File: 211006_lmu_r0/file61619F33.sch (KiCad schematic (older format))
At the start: 28 parts

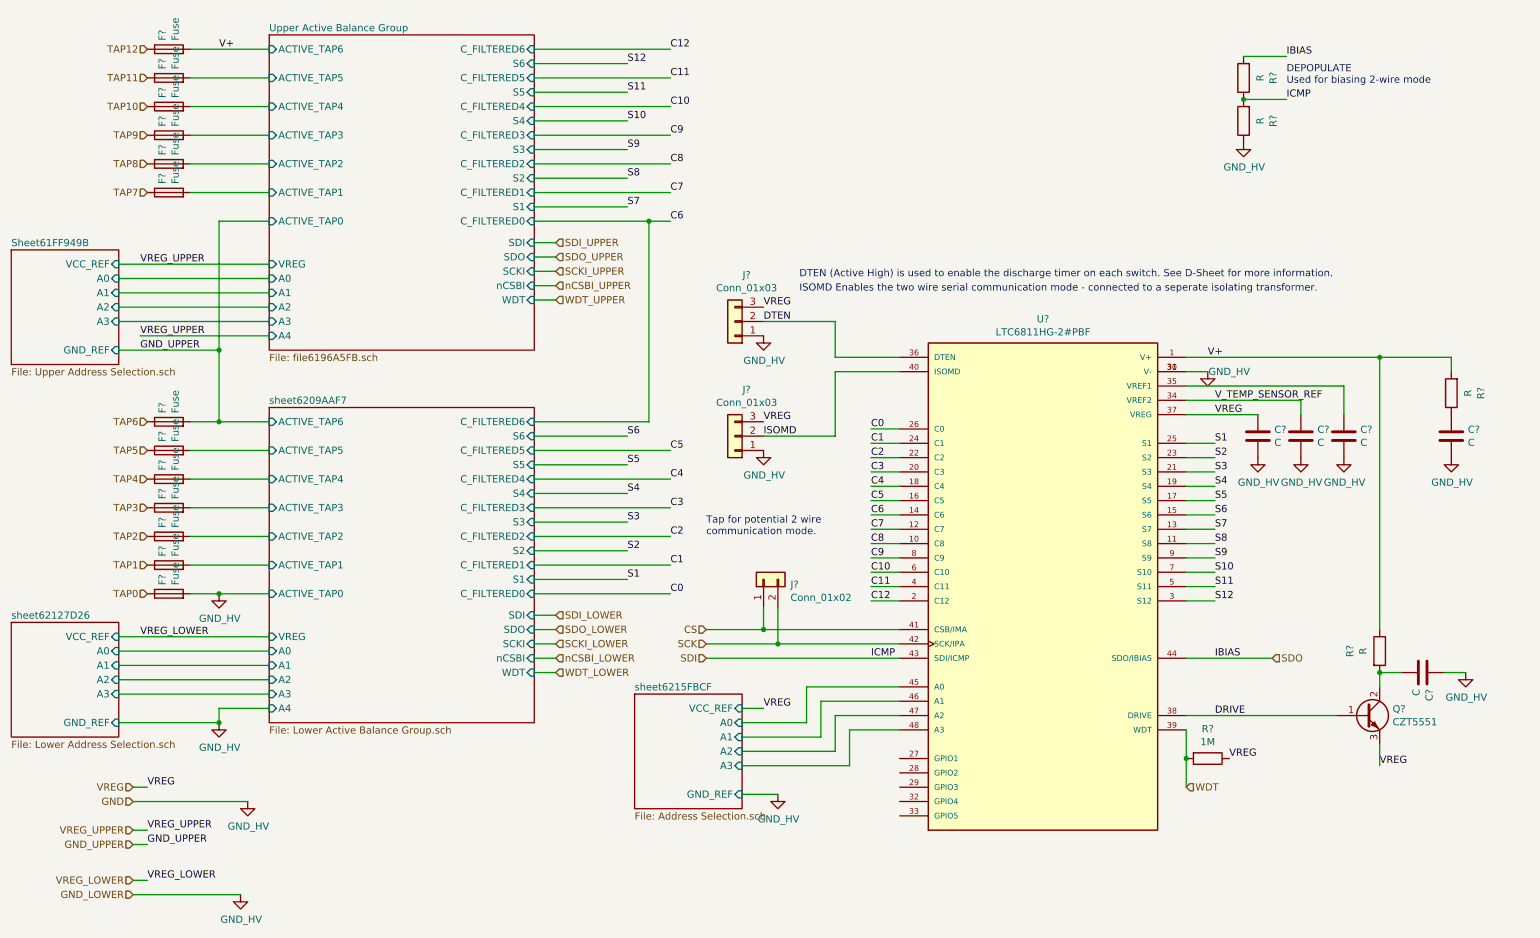
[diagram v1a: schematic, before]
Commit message: Updated BOM and footprints for non-hv components
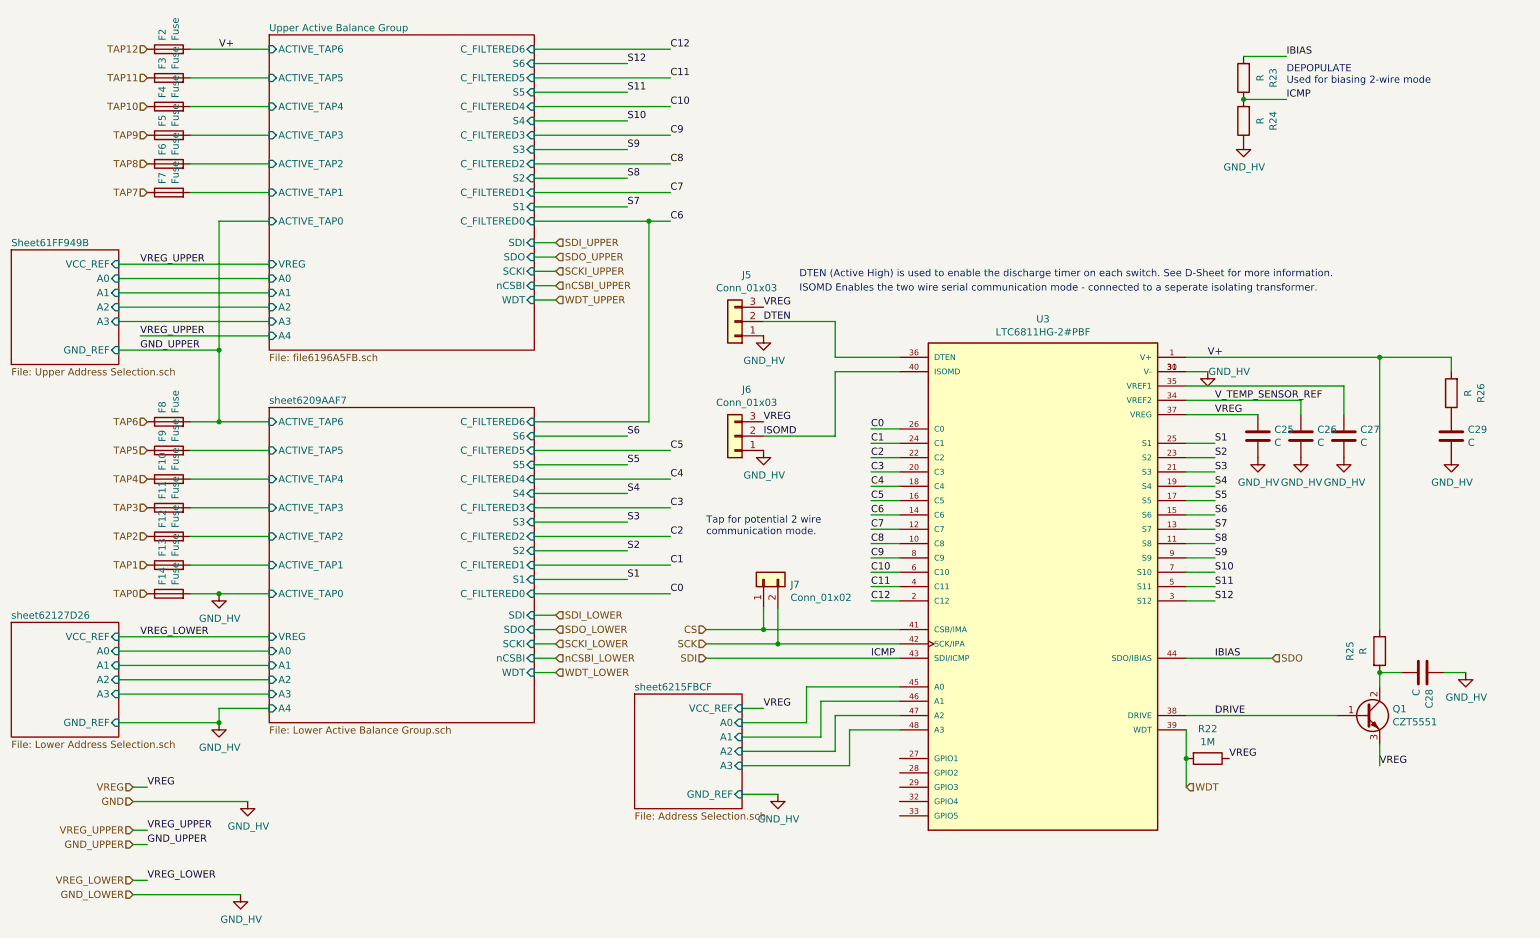
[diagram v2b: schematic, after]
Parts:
- gave numbers to parts that had none: 28

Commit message: Added most footprint requirements in HV
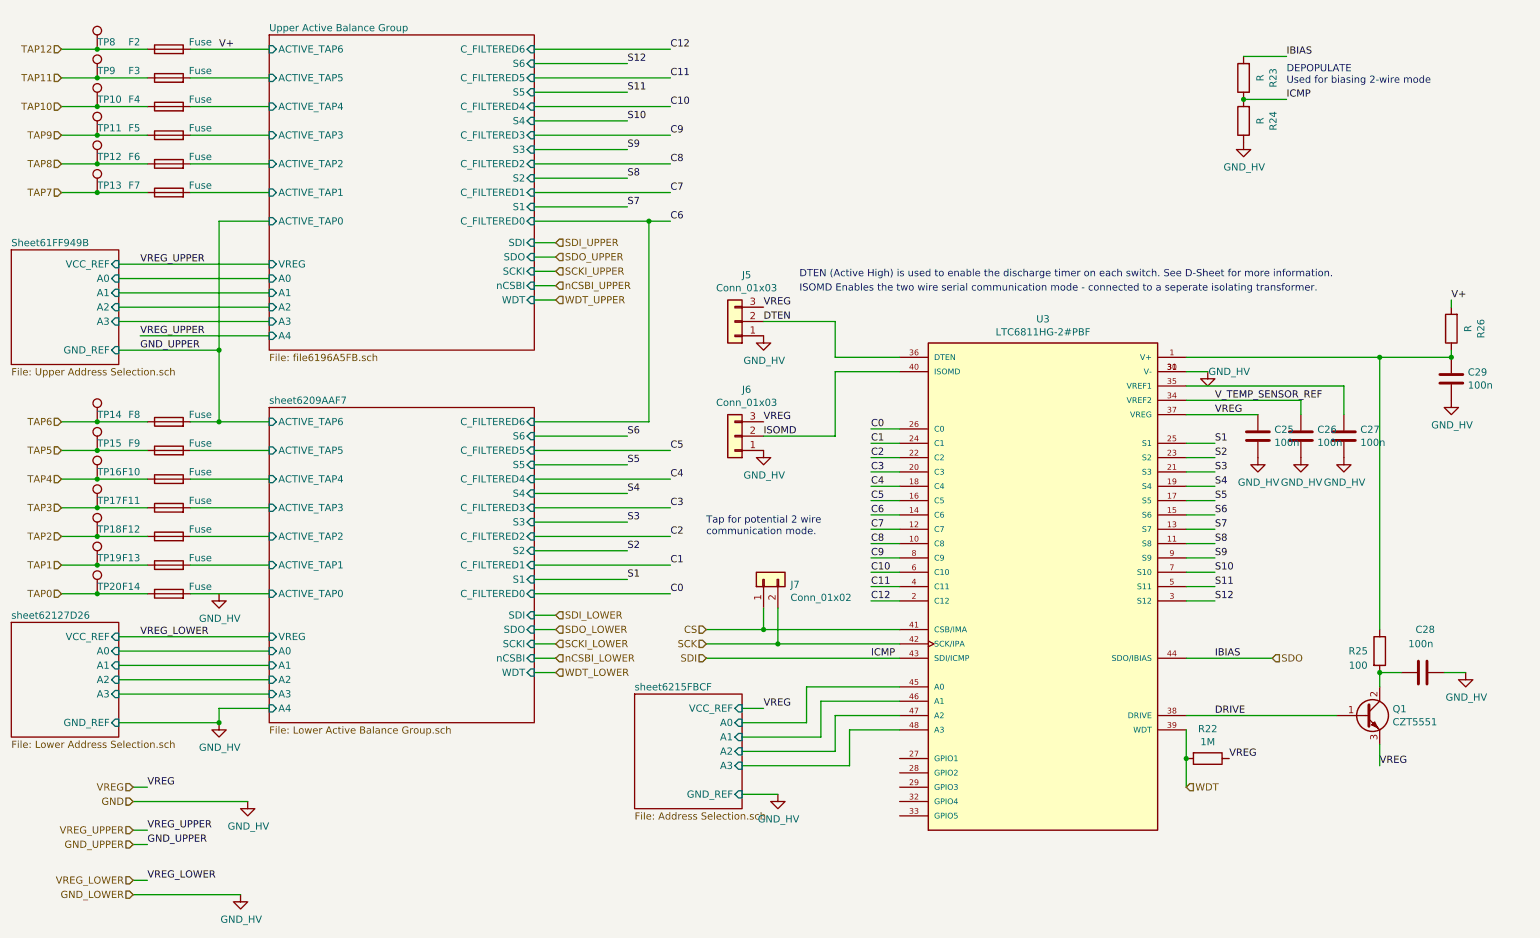
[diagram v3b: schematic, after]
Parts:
- added TP10, TP11, TP12, TP13, TP14, TP15, TP16, TP17, TP18, TP19, TP20, TP8, TP9: TestPoint, symbol Connector:TestPoint
- C25, C26, C27: value C -> 100n; footprint (none) -> Capacitor_SMD:C_0603_1608Metric_Pad1.08x0.95mm_HandSolder
- C28, C29: value C -> 100n; footprint (none) -> Capacitor_SMD:C_0805_2012Metric_Pad1.18x1.45mm_HandSolder
- F10, F11, F12, F13, F14, F2, F3, F4, F5, F6, F7, F8, F9: footprint (none) -> Fuse:Fuse_0805_2012Metric_Pad1.15x1.40mm_HandSolder
- J5, J6: footprint (none) -> Connector_PinHeader_2.54mm:PinHeader_1x03_P2.54mm_Vertical
- J7: footprint (none) -> Connector_PinHeader_2.54mm:PinHeader_1x02_P2.54mm_Vertical
- R22: footprint (none) -> Resistor_SMD:R_0603_1608Metric_Pad0.98x0.95mm_HandSolder
- R25: value R -> 100; footprint (none) -> Resistor_SMD:R_1206_3216Metric_Pad1.30x1.75mm_HandSolder
- R26: footprint (none) -> Resistor_SMD:R_1206_3216Metric_Pad1.30x1.75mm_HandSolder
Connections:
- net GND: no longer F14.2
- net TAP0: now also TP20.1
- net TAP1: now also TP19.1
- net TAP10: now also TP10.1
- net TAP11: now also TP9.1
- net TAP12: now also TP8.1
- net TAP2: now also TP18.1
- net TAP3: now also TP17.1
- net TAP4: now also TP16.1
- net TAP5: now also TP15.1
- net TAP6: now also TP14.1
- net TAP7: now also TP13.1
- net TAP8: now also TP12.1
- net TAP9: now also TP11.1
- net V+: no longer R25.1, U3.1 (V+)
- net at C29.1, R26.1: now also R25.1, U3.1 (V+)
- new net sheet6209AAF7/ACTIVE_TAP0: F14.2
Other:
- moved on the sheet: C29, R26

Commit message: Cleaned up last components missing footprint refs
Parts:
- R23, R24: footprint (none) -> Resistor_SMD:R_0805_2012Metric_Pad1.20x1.40mm_HandSolder
- TP10, TP11, TP12, TP13, TP14, TP15, TP16, TP17, TP18, TP19, TP20, TP8, TP9: footprint (none) -> TestPoint:TestPoint_Pad_D1.0mm
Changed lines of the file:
@@
 F 0 "R23" V 9093 1150 50  0000 C CNN
 F 1 "R" V 9184 1150 50  0000 C CNN
-F 2 "" V 9230 1150 50  0001 C CNN
+F 2 "Resistor_SMD:R_0805_2012Metric_Pad1.20x1.40mm_HandSolder" V 9230 1150 50  0001 C CNN
 F 3 "~" H 9300 1150 50  0001 C CNN
 	1    9300 1150
@@
 F 0 "R24" V 9093 1450 50  0000 C CNN
 F 1 "R" V 9184 1450 50  0000 C CNN
-F 2 "" V 9230 1450 50  0001 C CNN
+F 2 "Resistor_SMD:R_0805_2012Metric_Pad1.20x1.40mm_HandSolder" V 9230 1450 50  0001 C CNN
 F 3 "~" H 9300 1450 50  0001 C CNN
 	1    9300 1450
@@
 F 0 "TP8" H 1300 1000 50  0000 L CNN
 F 1 "TestPoint" H 1358 977 50  0001 L CNN
-F 2 "" H 1500 950 50  0001 C CNN
+F 2 "TestPoint:TestPoint_Pad_D1.0mm" H 1500 950 50  0001 C CNN
 F 3 "~" H 1500 950 50  0001 C CNN
 	1    1300 950
@@
 F 0 "TP9" H 1300 1200 50  0000 L CNN
 F 1 "TestPoint" H 1358 1177 50  0001 L CNN
-F 2 "" H 1500 1150 50  0001 C CNN
+F 2 "TestPoint:TestPoint_Pad_D1.0mm" H 1500 1150 50  0001 C CNN
 F 3 "~" H 1500 1150 50  0001 C CNN
 	1    1300 1150
@@
 F 0 "TP10" H 1300 1400 50  0000 L CNN
 F 1 "TestPoint" H 1358 1377 50  0001 L CNN
-F 2 "" H 1500 1350 50  0001 C CNN
+F 2 "TestPoint:TestPoint_Pad_D1.0mm" H 1500 1350 50  0001 C CNN
 F 3 "~" H 1500 1350 50  0001 C CNN
 	1    1300 1350
@@
 F 0 "TP11" H 1300 1600 50  0000 L CNN
 F 1 "TestPoint" H 1358 1577 50  0001 L CNN
-F 2 "" H 1500 1550 50  0001 C CNN
+F 2 "TestPoint:TestPoint_Pad_D1.0mm" H 1500 1550 50  0001 C CNN
 F 3 "~" H 1500 1550 50  0001 C CNN
 	1    1300 1550
@@
 F 0 "TP12" H 1300 1800 50  0000 L CNN
 F 1 "TestPoint" H 1358 1777 50  0001 L CNN
-F 2 "" H 1500 1750 50  0001 C CNN
+F 2 "TestPoint:TestPoint_Pad_D1.0mm" H 1500 1750 50  0001 C CNN
 F 3 "~" H 1500 1750 50  0001 C CNN
 	1    1300 1750
@@
 F 0 "TP13" H 1300 2000 50  0000 L CNN
 F 1 "TestPoint" H 1358 1977 50  0001 L CNN
-F 2 "" H 1500 1950 50  0001 C CNN
+F 2 "TestPoint:TestPoint_Pad_D1.0mm" H 1500 1950 50  0001 C CNN
 F 3 "~" H 1500 1950 50  0001 C CNN
 	1    1300 1950
@@
 F 0 "TP14" H 1300 3600 50  0000 L CNN
 F 1 "TestPoint" H 1358 3577 50  0001 L CNN
-F 2 "" H 1500 3550 50  0001 C CNN
+F 2 "TestPoint:TestPoint_Pad_D1.0mm" H 1500 3550 50  0001 C CNN
 F 3 "~" H 1500 3550 50  0001 C CNN
 	1    1300 3550
@@
 F 0 "TP15" H 1300 3800 50  0000 L CNN
 F 1 "TestPoint" H 1358 3777 50  0001 L CNN
-F 2 "" H 1500 3750 50  0001 C CNN
+F 2 "TestPoint:TestPoint_Pad_D1.0mm" H 1500 3750 50  0001 C CNN
 F 3 "~" H 1500 3750 50  0001 C CNN
 	1    1300 3750
@@
 F 0 "TP16" H 1300 4000 50  0000 L CNN
 F 1 "TestPoint" H 1358 3977 50  0001 L CNN
-F 2 "" H 1500 3950 50  0001 C CNN
+F 2 "TestPoint:TestPoint_Pad_D1.0mm" H 1500 3950 50  0001 C CNN
 F 3 "~" H 1500 3950 50  0001 C CNN
 	1    1300 3950
@@
 F 0 "TP17" H 1300 4200 50  0000 L CNN
 F 1 "TestPoint" H 1358 4177 50  0001 L CNN
-F 2 "" H 1500 4150 50  0001 C CNN
+F 2 "TestPoint:TestPoint_Pad_D1.0mm" H 1500 4150 50  0001 C CNN
 F 3 "~" H 1500 4150 50  0001 C CNN
 	1    1300 4150
@@
 F 0 "TP18" H 1300 4400 50  0000 L CNN
 F 1 "TestPoint" H 1358 4377 50  0001 L CNN
-F 2 "" H 1500 4350 50  0001 C CNN
+F 2 "TestPoint:TestPoint_Pad_D1.0mm" H 1500 4350 50  0001 C CNN
 F 3 "~" H 1500 4350 50  0001 C CNN
 	1    1300 4350
@@
 F 0 "TP19" H 1300 4600 50  0000 L CNN
 F 1 "TestPoint" H 1358 4577 50  0001 L CNN
-F 2 "" H 1500 4550 50  0001 C CNN
+F 2 "TestPoint:TestPoint_Pad_D1.0mm" H 1500 4550 50  0001 C CNN
 F 3 "~" H 1500 4550 50  0001 C CNN
 	1    1300 4550
@@
 F 0 "TP20" H 1300 4800 50  0000 L CNN
 F 1 "TestPoint" H 1358 4777 50  0001 L CNN
-F 2 "" H 1500 4750 50  0001 C CNN
+F 2 "TestPoint:TestPoint_Pad_D1.0mm" H 1500 4750 50  0001 C CNN
 F 3 "~" H 1500 4750 50  0001 C CNN
 	1    1300 4750

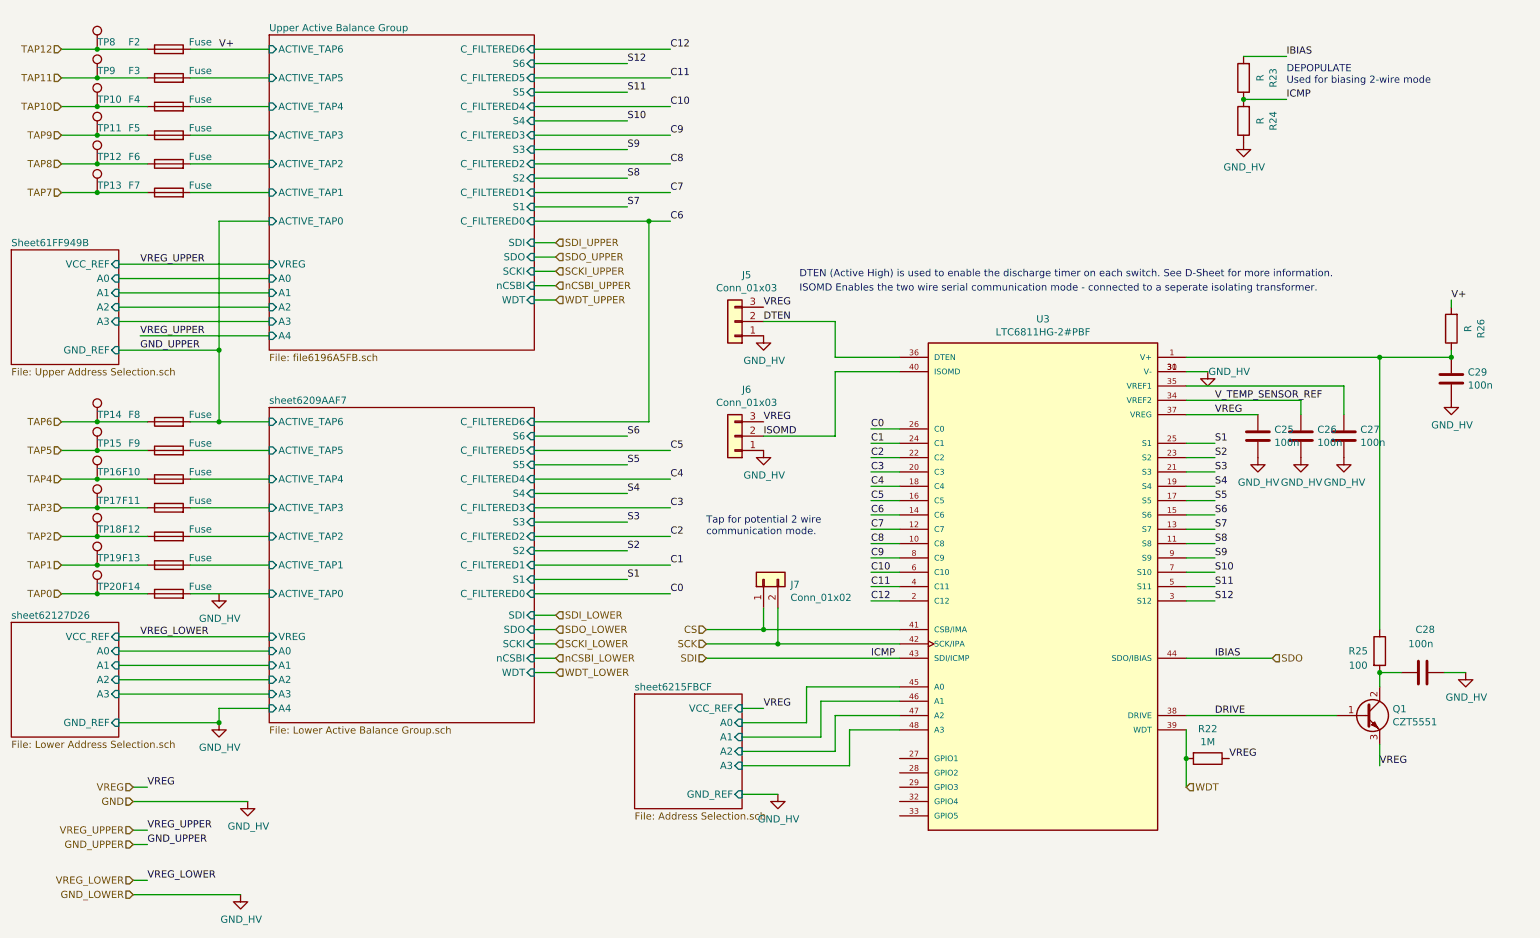
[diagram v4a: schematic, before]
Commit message: Updated with Mouser links for BOM
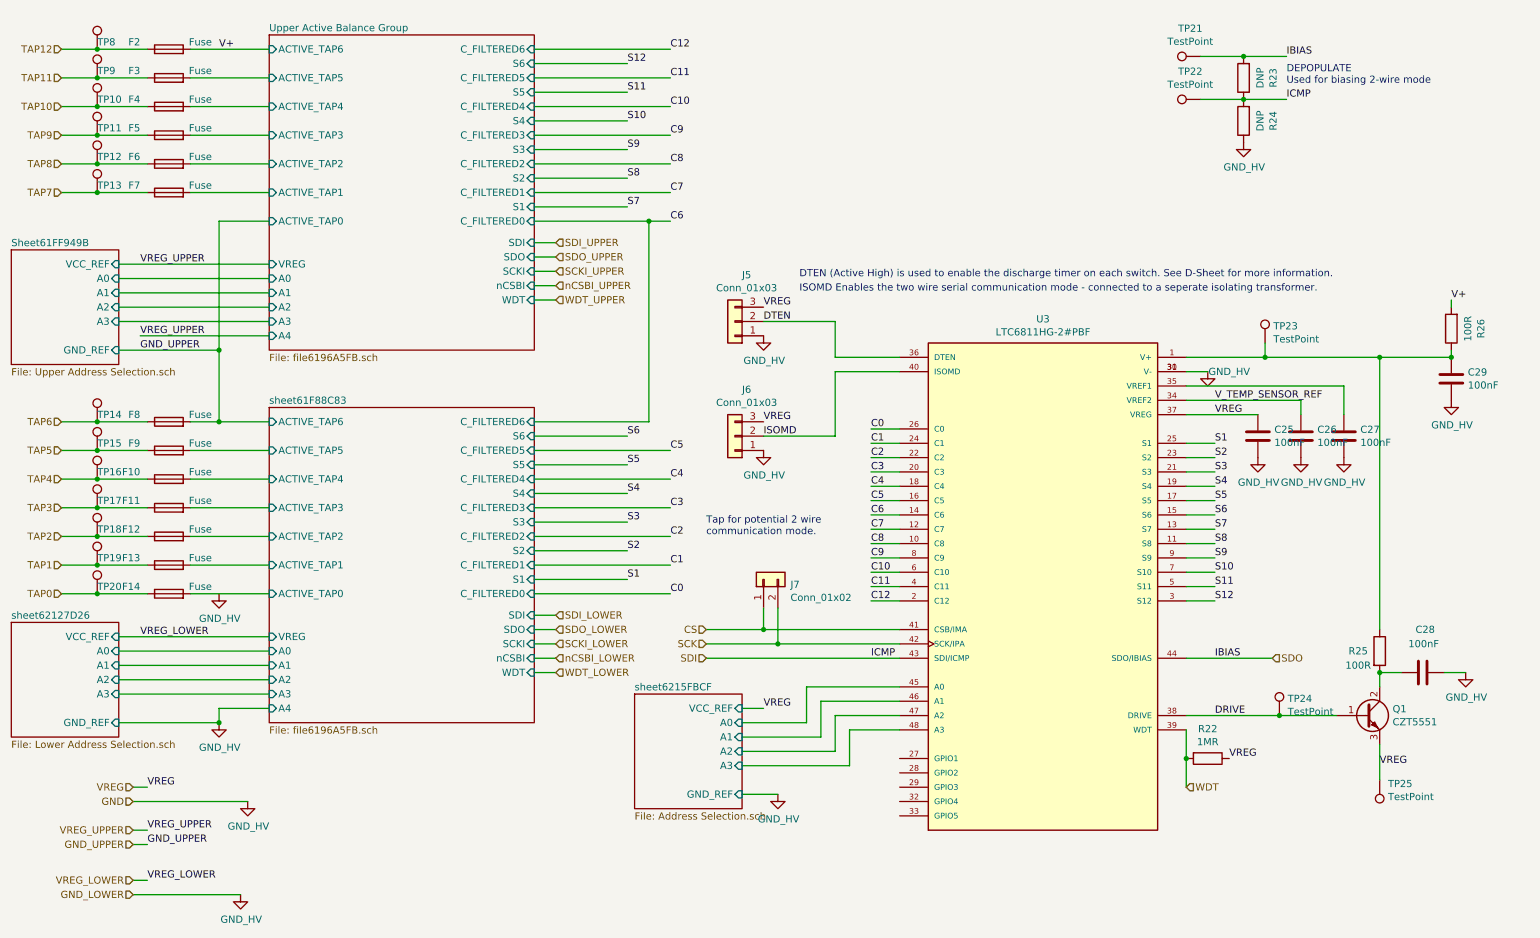
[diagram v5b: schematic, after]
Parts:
- added TP21, TP22, TP23, TP24, TP25: TestPoint, TestPoint:TestPoint_Pad_D1.0mm, symbol Connector:TestPoint
- C25, C26, C27, C28, C29: value 100n -> 100nF
- F10, F11, F12, F13, F14, F2, F3, F4, F5, F6, F7, F8, F9: Manufacturer (none) -> Vishay; Mouser Part Number (none) -> 594-MFU0805FF04000P1; Mouser URL (none) -> https://au.mouser.com/ProductDetail/Vishay-Beyschlag/MFU080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; Part Number (none) -> MFU0805FF04000P100
- Q1: Manufacturer (none) -> Central Semiconductor; Mouser Part Number (none) -> 610-CZT5551; Mouser URL (none) -> https://au.mouser.com/ProductDetail/Central-Semiconductor/C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; Part Number (none) -> CZT5551
- R22: value 1M -> 1MR
- R23, R24: value R -> DNP
- R25: value 100 -> 100R
- R26: value R -> 100R
- TP10, TP11, TP12, TP13, TP14, TP15, TP16, TP17, TP18, TP19, TP20, TP8, TP9: Manufacturer (none) -> -; Mouser Part Number (none) -> -; Mouser URL (none) -> -; Part Number (none) -> -
- U3: MANUFACTURER Linear Technology -> (none); Manufacturer (none) -> Linear Technology; Mouser Part Number (none) -> NOT AVAILABLE!; Mouser URL (none) -> NOT AVAILABLE!; Part Number (none) -> LTC6811HG-2#PBF
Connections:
- net DRIVE: now also TP24.1
- net SDI: now also TP22.1
- net SDO: now also TP21.1
- net VREG: now also TP25.1
- net at C29.1, R25.1, R26.1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: now also TP23.1
- net sheet6209AAF7/ACTIVE_TAP0 renamed sheet61F88C83/ACTIVE_TAP0
- net sheet6209AAF7/ACTIVE_TAP1 renamed sheet61F88C83/ACTIVE_TAP1
- net sheet6209AAF7/ACTIVE_TAP2 renamed sheet61F88C83/ACTIVE_TAP2
- net sheet6209AAF7/ACTIVE_TAP3 renamed sheet61F88C83/ACTIVE_TAP3
- net sheet6209AAF7/ACTIVE_TAP4 renamed sheet61F88C83/ACTIVE_TAP4
- net sheet6209AAF7/ACTIVE_TAP5 renamed sheet61F88C83/ACTIVE_TAP5
